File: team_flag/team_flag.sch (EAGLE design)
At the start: 7 parts, among them Q1 MOSFET-NCHANNELSMD, Q2 MOSFET-NCHANNELSMD

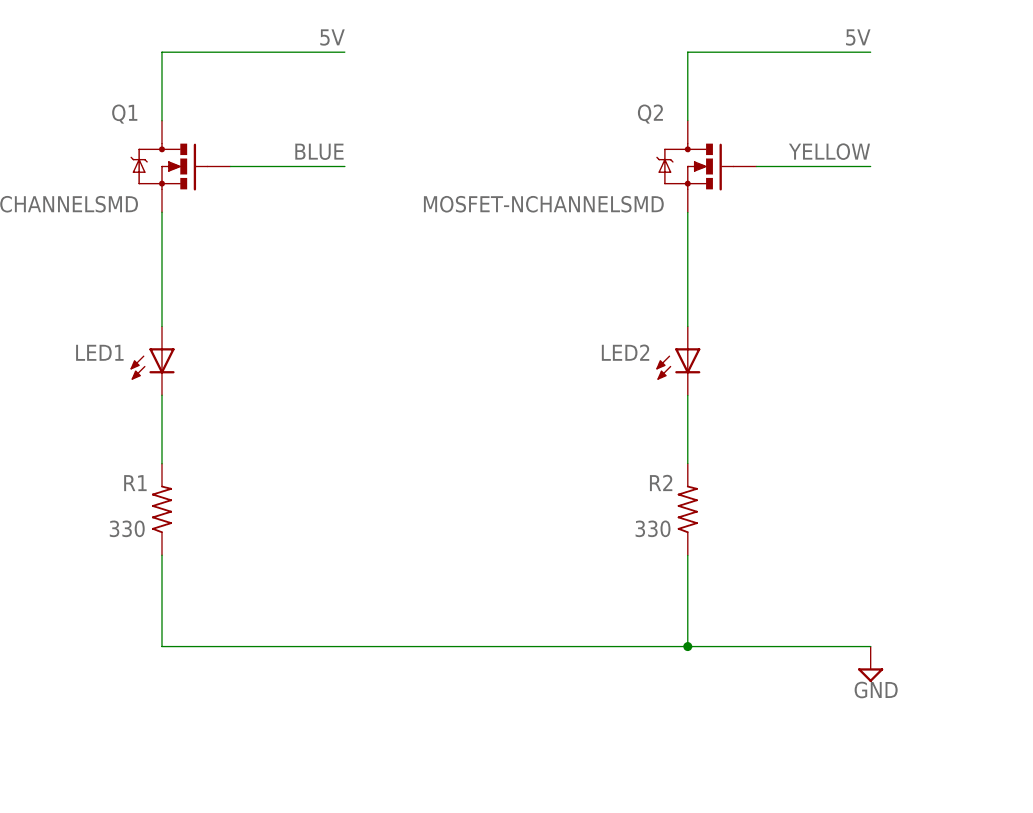
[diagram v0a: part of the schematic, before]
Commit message: Team Flag pull down resistors
-Added pull down resistors to fix issue with LEDs
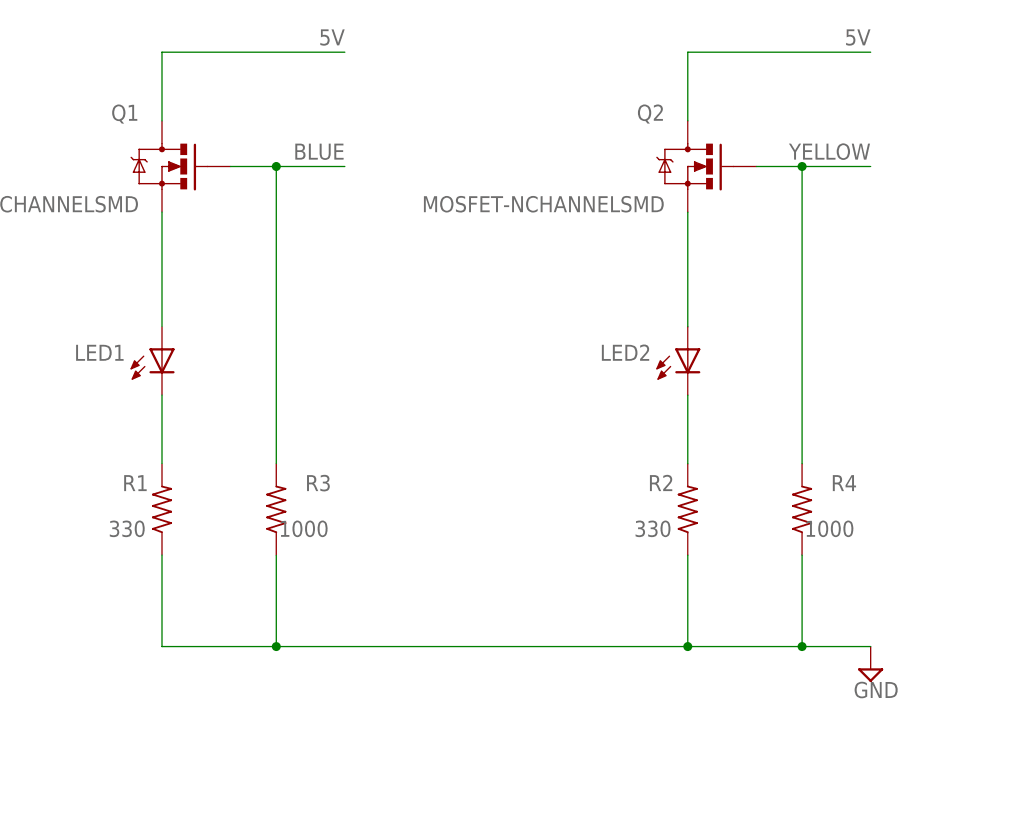
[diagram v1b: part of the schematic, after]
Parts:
- added R3, R4: 1000, rcl:R-US_R0603
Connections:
- net BLUE: now also R3.2
- net GND: now also R3.1, R4.1
- net YELLOW: now also R4.2
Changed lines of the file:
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@@
 <attribute name="REVISION" value="B"/>
 </part>
+<part name="R3" library="rcl" deviceset="R-US_" device="R0603" value="1000"/>
+<part name="R4" library="rcl" deviceset="R-US_" device="R0603" value="1000"/>
 </parts>
 <sheets>
@@
 <attribute name="REVISION" x="147.32" y="0" size="1.778" layer="96" display="off"/>
 </instance>
+<instance part="R3" gate="G$1" x="53.34" y="38.1" smashed="yes" rot="R90">
+<attribute name="NAME" x="59.4614" y="41.91" size="1.778" layer="95" rot="R180"/>
+<attribute name="VALUE" x="59.182" y="36.83" size="1.778" layer="96" rot="R180"/>
+</instance>
+<instance part="R4" gate="G$1" x="111.76" y="38.1" smashed="yes" rot="R90">
+<attribute name="NAME" x="117.8814" y="41.91" size="1.778" layer="95" rot="R180"/>
+<attribute name="VALUE" x="117.602" y="36.83" size="1.778" layer="96" rot="R180"/>
+</instance>
 </instances>
 <busses>
@@
 <segment>
 <pinref part="Q2" gate="G$1" pin="G"/>
-<wire x1="106.68" y1="76.2" x2="119.38" y2="76.2" width="0.1524" layer="91"/>
+<wire x1="106.68" y1="76.2" x2="111.76" y2="76.2" width="0.1524" layer="91"/>
 <label x="119.38" y="78.74" size="1.778" layer="95" rot="R180"/>
+<junction x="111.76" y="76.2"/>
+<wire x1="111.76" y1="76.2" x2="119.38" y2="76.2" width="0.1524" layer="91"/>
+<pinref part="R4" gate="G$1" pin="2"/>
+<wire x1="111.76" y1="76.2" x2="111.76" y2="43.18" width="0.1524" layer="91"/>
 </segment>
 </net>
@@
 <pinref part="R2" gate="G$1" pin="1"/>
 <wire x1="40.64" y1="33.02" x2="40.64" y2="22.86" width="0.1524" layer="91"/>
-<wire x1="40.64" y1="22.86" x2="99.06" y2="22.86" width="0.1524" layer="91"/>
+<wire x1="40.64" y1="22.86" x2="53.34" y2="22.86" width="0.1524" layer="91"/>
+<wire x1="53.34" y1="22.86" x2="99.06" y2="22.86" width="0.1524" layer="91"/>
 <wire x1="99.06" y1="22.86" x2="99.06" y2="33.02" width="0.1524" layer="91"/>
-<wire x1="99.06" y1="22.86" x2="119.38" y2="22.86" width="0.1524" layer="91"/>
+<wire x1="99.06" y1="22.86" x2="111.76" y2="22.86" width="0.1524" layer="91"/>
 <pinref part="SUPPLY1" gate="GND" pin="GND"/>
 <junction x="99.06" y="22.86"/>
+<junction x="53.34" y="22.86"/>
+<junction x="111.76" y="22.86"/>
+<wire x1="111.76" y1="22.86" x2="119.38" y2="22.86" width="0.1524" layer="91"/>
+<pinref part="R3" gate="G$1" pin="1"/>
+<wire x1="53.34" y1="22.86" x2="53.34" y2="33.02" width="0.1524" layer="91"/>
+<pinref part="R4" gate="G$1" pin="1"/>
+<wire x1="111.76" y1="33.02" x2="111.76" y2="22.86" width="0.1524" layer="91"/>
 </segment>
 <segment>
@@
 <segment>
 <pinref part="Q1" gate="G$1" pin="G"/>
-<wire x1="48.26" y1="76.2" x2="60.96" y2="76.2" width="0.1524" layer="91"/>
+<wire x1="48.26" y1="76.2" x2="53.34" y2="76.2" width="0.1524" layer="91"/>
 <label x="60.96" y="78.74" size="1.778" layer="95" rot="R180"/>
+<wire x1="53.34" y1="76.2" x2="60.96" y2="76.2" width="0.1524" layer="91"/>
+<wire x1="53.34" y1="76.2" x2="53.34" y2="43.18" width="0.1524" layer="91"/>
+<junction x="53.34" y="76.2"/>
+<pinref part="R3" gate="G$1" pin="2"/>
 </segment>
 <segment>

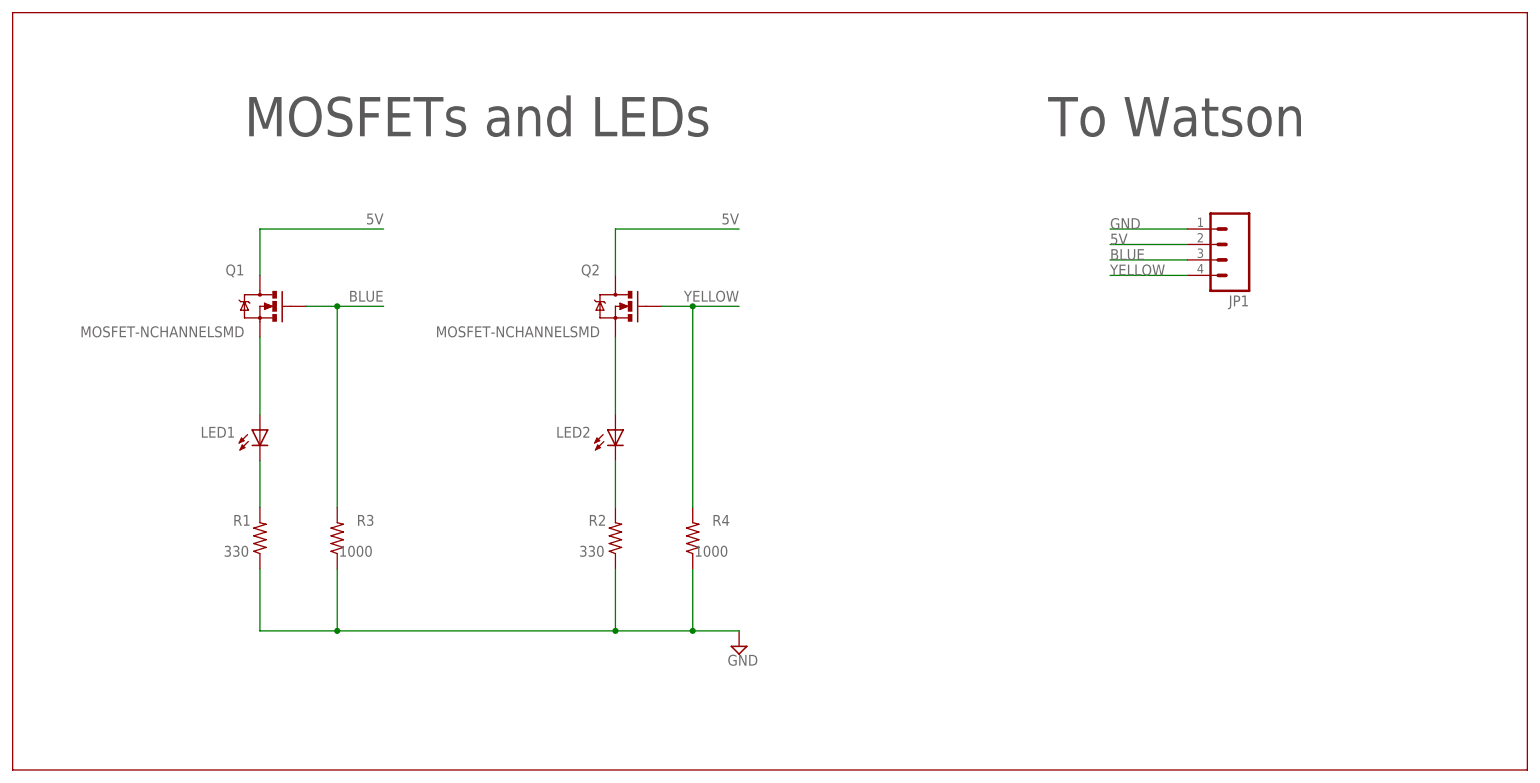
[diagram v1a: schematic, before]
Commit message: Team Flag new mosfets
-replaced old mosfets with logic-level mosfets
-changed pull down resistor value to 10K
-renamed 5V signal to VCC
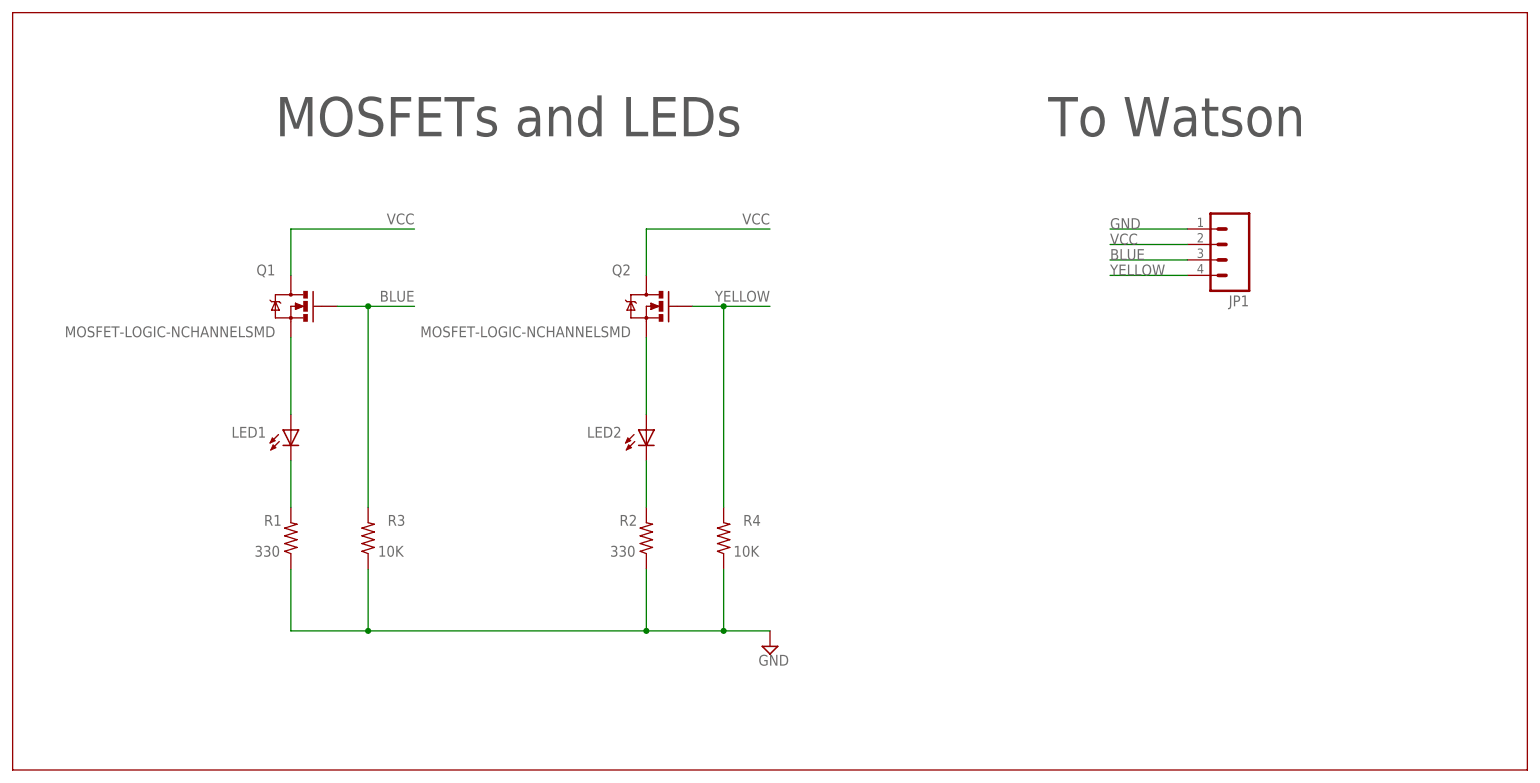
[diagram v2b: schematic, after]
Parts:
- Q1, Q2: value MOSFET-NCHANNELSMD -> MOSFET-LOGIC-NCHANNELSMD; device pie:MOSFET-NCHANNELSMD -> pie:MOSFET-LOGIC-NCHANNELSMD
- R3, R4: value 1000 -> 10K
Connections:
- net 5V renamed VCC
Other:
- moved on the sheet: LED1, LED2, Q1, Q2, R1, R2, R3, R4
